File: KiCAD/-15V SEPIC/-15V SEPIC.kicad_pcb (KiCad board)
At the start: 4 copper layers, 24 x 30 mm, 21 parts, among them J1 Conn_01x04_Pin, U1 LT3579

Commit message: kicad sepic update
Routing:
- net GND: vias 75 -> 52
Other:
- board text added: "AUDIO DSP"
- board text added: "JLCJLCJLCJLC"
- board text added: "SEPIC -15V"

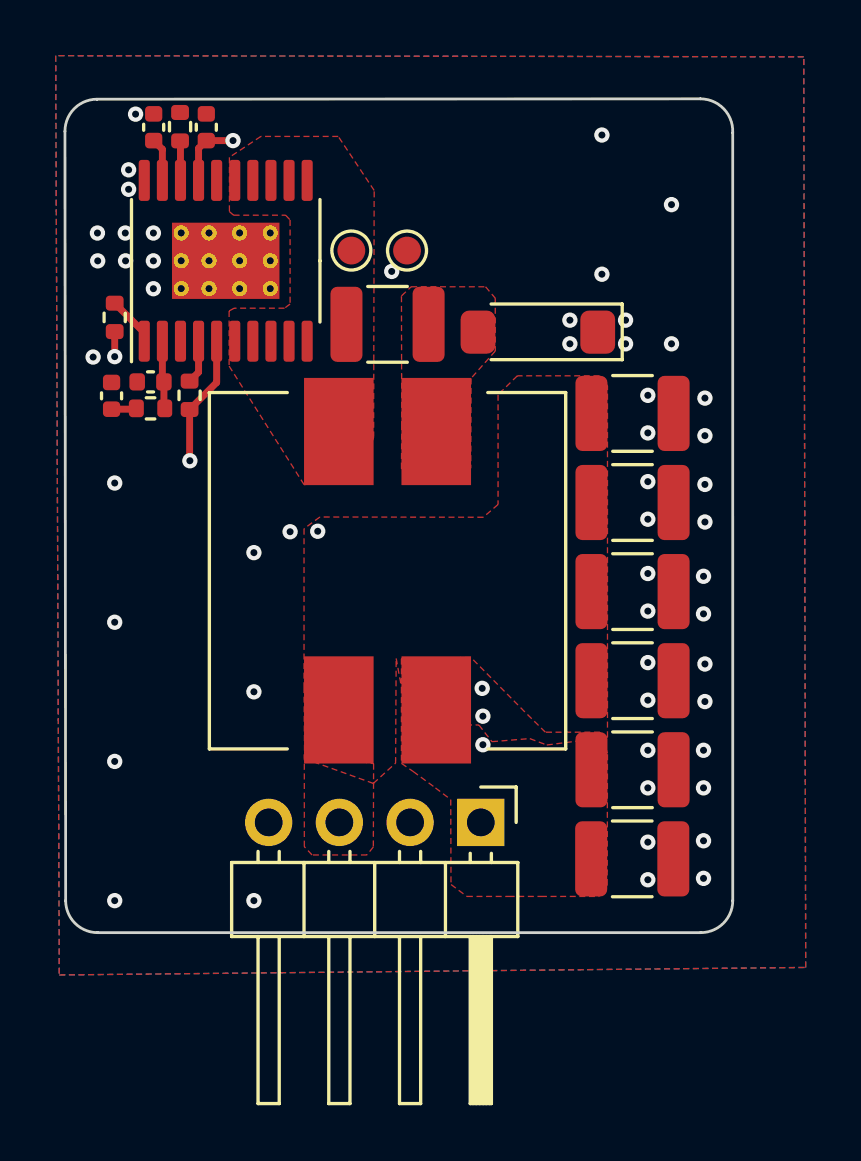
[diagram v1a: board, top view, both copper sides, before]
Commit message: Added SEPIC symbol and footprint and worked on main board
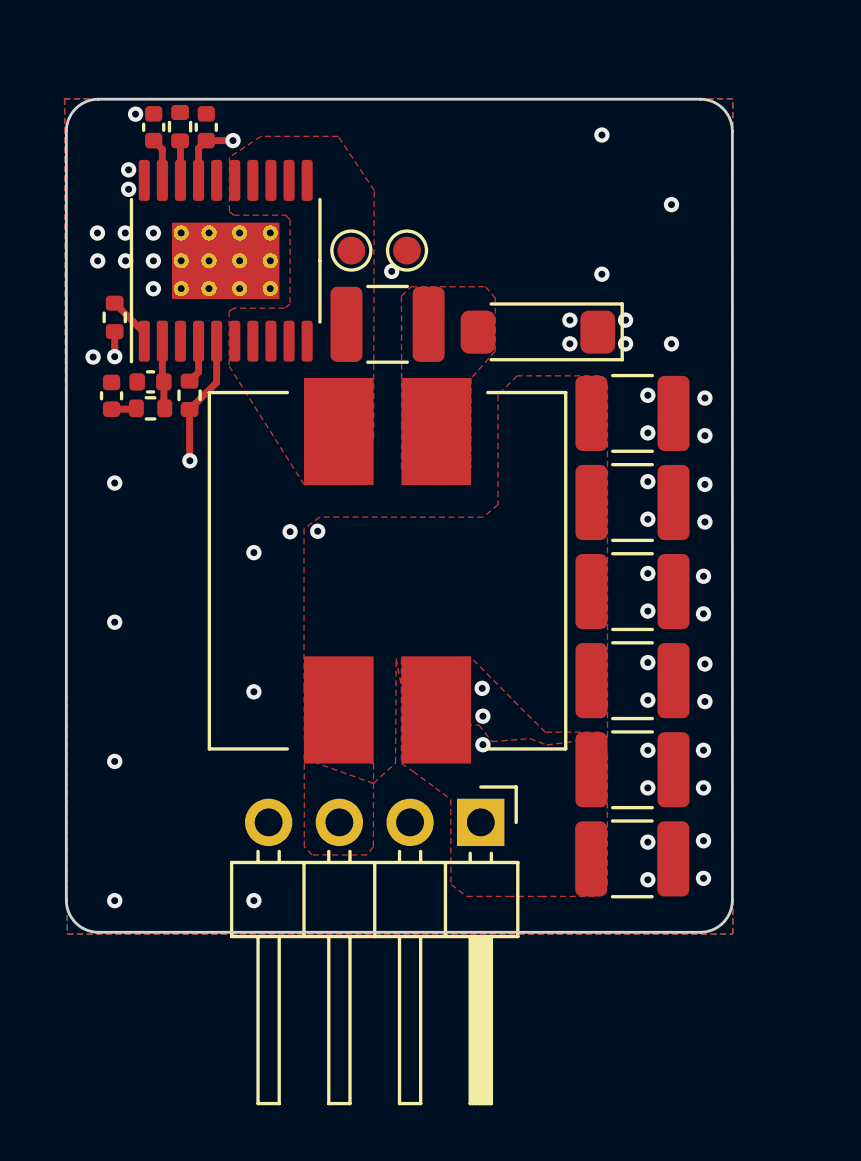
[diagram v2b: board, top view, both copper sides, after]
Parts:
- J1: value Conn_01x04_Pin -> Conn_01x04
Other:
- board size 24 x 30 mm -> 23.9 x 29.9 mm
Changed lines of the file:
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@@
     (property "Sheetfile" "-15V SEPIC.kicad_sch")
     (property "Sheetname" "")
-    (property "ki_description" "Generic connector, single row, 01x04, script generated")
+    (property "ki_description" "Generic connector, single row, 01x04, script generated (kicad-library-utils/schlib/autogen/connector/)")
     (property "ki_keywords" "connector")
     (attr through_hole)
@@
         (effects (font (size 1 1) (thickness 0.15)))
     )
-    (fp_text value "Conn_01x04_Pin" (at 4.385 9.89 90) (layer "F.Fab")
+    (fp_text value "Conn_01x04" (at 4.385 9.89 90) (layer "F.Fab")
         (effects (font (size 1 1) (thickness 0.15)))
     )
@@
     )
   )
-  (gr_line (start 77.198853 59.914819) (end 77.2 87.5)
+  (gr_line (start 77.186827 59.863173) (end 77.186827 87.486827)
     (stroke (width 0.1) (type default)) (layer "Edge.Cuts"))
-  (gr_arc (start 76.036827 58.7) (mid 76.877376 59.059152) (end 77.198853 59.914819)
+  (gr_arc (start 54.413173 88.636827) (mid 53.6 88.3) (end 53.263173 87.486827)
     (stroke (width 0.1) (type default)) (layer "Edge.Cuts"))
-  (gr_arc (start 77.2 87.5) (mid 76.863173 88.313173) (end 76.05 88.65)
+  (gr_line (start 54.413173 58.713173) (end 76.036827 58.713173)
     (stroke (width 0.1) (type default)) (layer "Edge.Cuts"))
-  (gr_line (start 54.363173 58.713173) (end 76.036827 58.7)
+  (gr_arc (start 76.036827 58.713173) (mid 76.85 59.05) (end 77.186827 59.863173)
     (stroke (width 0.1) (type default)) (layer "Edge.Cuts"))
-  (gr_arc (start 54.388173 88.65) (mid 53.575 88.313173) (end 53.238173 87.5)
+  (gr_line (start 53.263173 87.486827) (end 53.263173 59.863173)
     (stroke (width 0.1) (type default)) (layer "Edge.Cuts"))
-  (gr_arc (start 53.213173 59.863173) (mid 53.55 59.05) (end 54.363173 58.713173)
+  (gr_arc (start 53.263173 59.863173) (mid 53.6 59.05) (end 54.413173 58.713173)
     (stroke (width 0.1) (type default)) (layer "Edge.Cuts"))
-  (gr_line (start 53.238173 87.5) (end 53.213173 59.863173)
+  (gr_line (start 76.036827 88.636827) (end 54.413173 88.636827)
     (stroke (width 0.1) (type default)) (layer "Edge.Cuts"))
-  (gr_line (start 76.05 88.65) (end 54.388173 88.65)
+  (gr_arc (start 77.186827 87.486827) (mid 76.85 88.3) (end 76.036827 88.636827)
     (stroke (width 0.1) (type default)) (layer "Edge.Cuts"))
   (gr_text "JLCJLCJLCJLC" (at 70.95 60.4) (layer "B.SilkS")
@@
     (polygon
       (pts
-        (xy 52.88 57.15)
-        (xy 53.01 90.17)
-        (xy 79.82 89.9)
-        (xy 79.75 57.19)
-      )
-    )
+        (xy 53.2 58.7)
+        (xy 53.3 88.7)
+        (xy 77.2 88.7)
+        (xy 77.2 58.7)
+      )
+    )
